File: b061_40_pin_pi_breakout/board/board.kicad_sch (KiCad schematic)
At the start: 15 parts, among them J1 SPI_2x3, J2 I2C_2x2, J3 UART, J4 SPI_2x3, J5 Conn_02x02_Odd_Even, J6 004_BASE-T_CT, J8 DebugEdge_02x05, J9 Raspberry_Pi_2_3

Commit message: connected int and status lines, now version 1.0
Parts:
- J1: value SPI_2x3 -> SPI
- J8: footprint on_edge:debug_edge_2x05_host -> on_edge:on_edge_2x05_host
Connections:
- net I2C0_CS: now reaches J2.4 (CS/EN)
- net I2C0_CS: now also J9.27 (ID_SD/GPIO0)
- net I2C0_INT: now reaches J2.5 (INT)
- net I2C0_INT: now also J9.28 (ID_SC/GPIO1)
- net I2C1_CS: now reaches J3.5 (INT)
- net I2C1_CS: now also J9.29 (GCLK1/GPIO5)
- net I2C1_INT: now reaches J3.6 (CS/EN)
- net I2C1_INT: now also J9.31 (GCLK2/GPIO6)
- net SPI0_INT: now reaches J1.5 (INT)
- net SPI0_INT: now also J9.32 (PWM0/GPIO12)
- net SPI0_Status: now reaches J1.7 (status)
- net SPI0_Status: now also J9.33 (PWM1/GPIO13)
- net SPI1_INT: now reaches J4.5 (INT)
- net SPI1_INT: now also J9.37 (GPIO26)
- net SPI1_Status: now reaches J4.7 (status)
- net SPI1_Status: now also J9.13 (GPIO27)
- no-connect marks 23 -> 7
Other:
- moved on the sheet: J4, R2

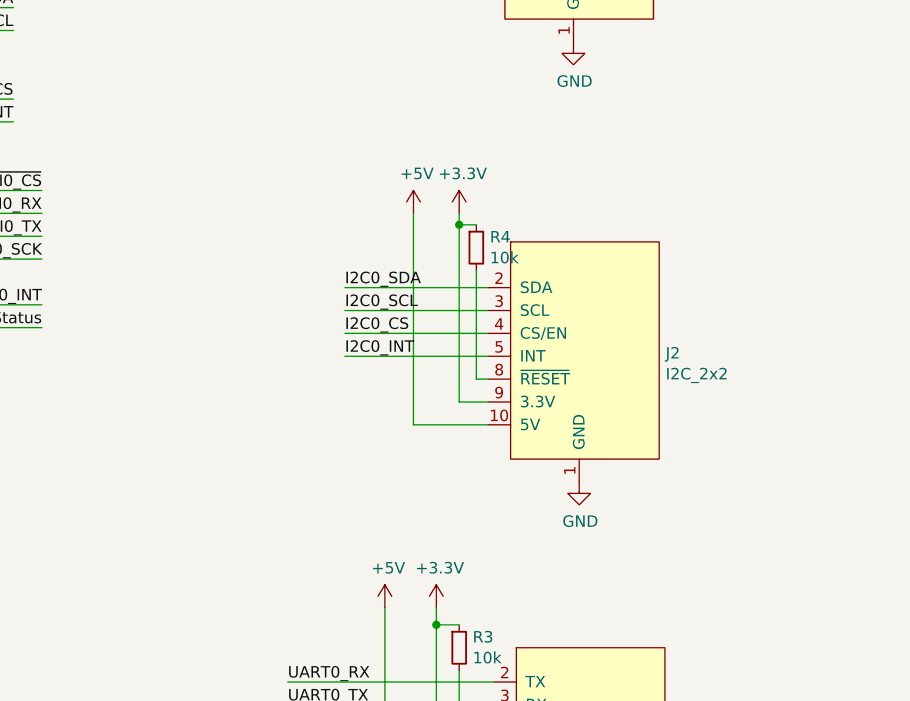
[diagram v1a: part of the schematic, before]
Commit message: added I2C pull ups, changed debug connector footprint, modernized to skinny slot connectors
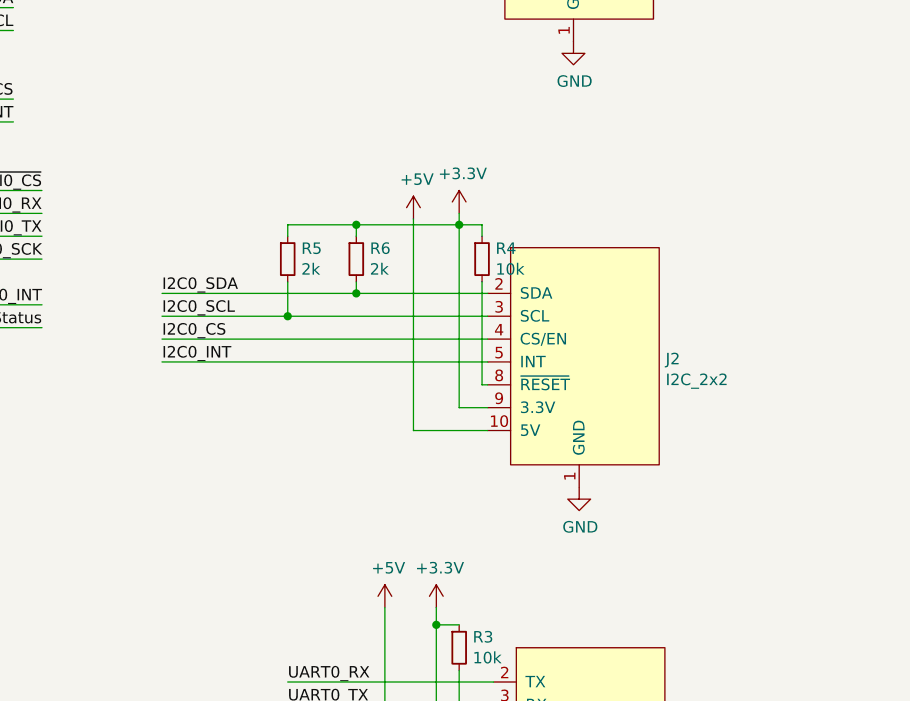
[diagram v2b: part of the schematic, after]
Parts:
- added R5, R6: 2k, Resistor_SMD:R_0603_1608Metric, symbol Device:R_Small
- J8: footprint on_edge:on_edge_2x05_host -> on_edge:debug_edge_2x05_host
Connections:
- net +3V3: now also R5.1, R6.1
- net I2C0_SCL: now also R5.2
- net I2C0_SDA: now also R6.2
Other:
- moved on the sheet: J2, R4
